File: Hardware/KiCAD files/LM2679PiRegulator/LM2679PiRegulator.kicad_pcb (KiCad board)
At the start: 2 copper layers, 48 x 48 mm, 14 parts, among them J2 Conn_01x03_Pin, U1 LM2679SX-5V

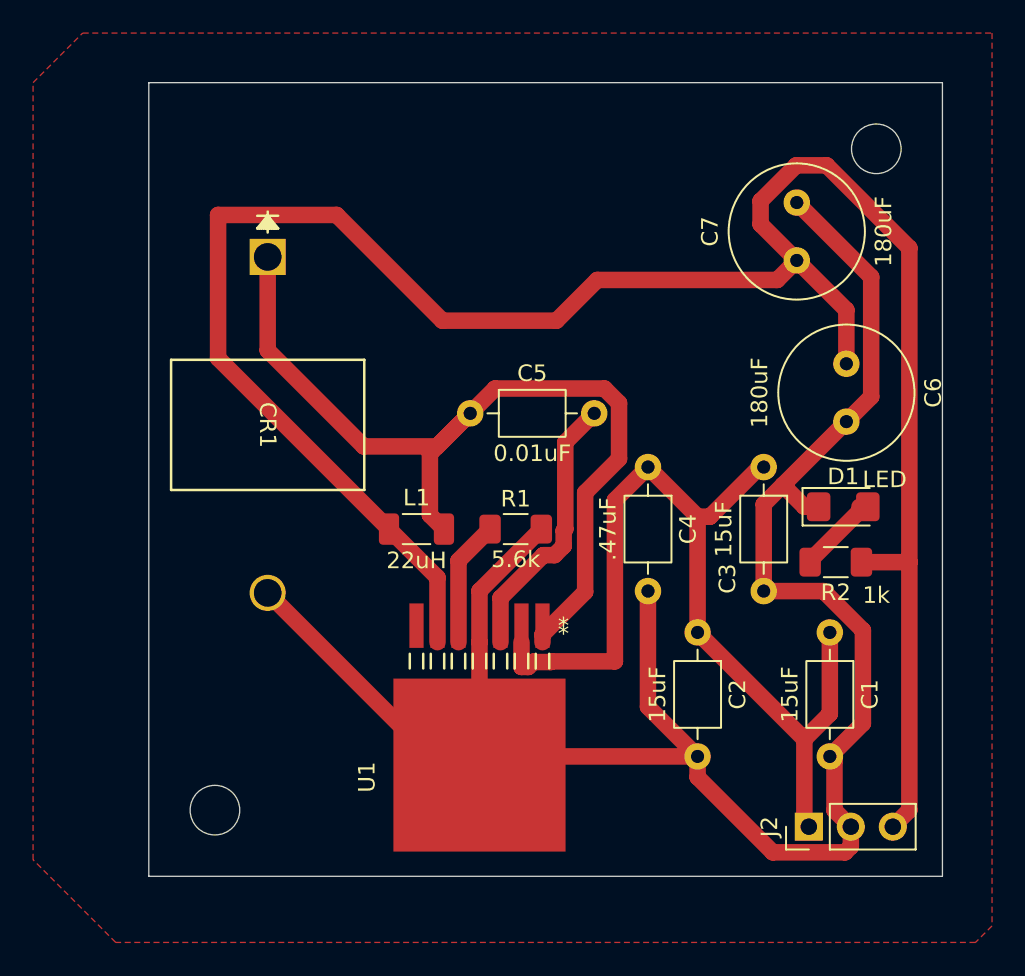
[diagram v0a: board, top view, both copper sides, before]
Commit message: 1st push of PCB's for printing
This is pre-peer review. This almost certainly has section that need adjustment. also realized I'm missing the USB-Uart bridge. first thing added in next version.
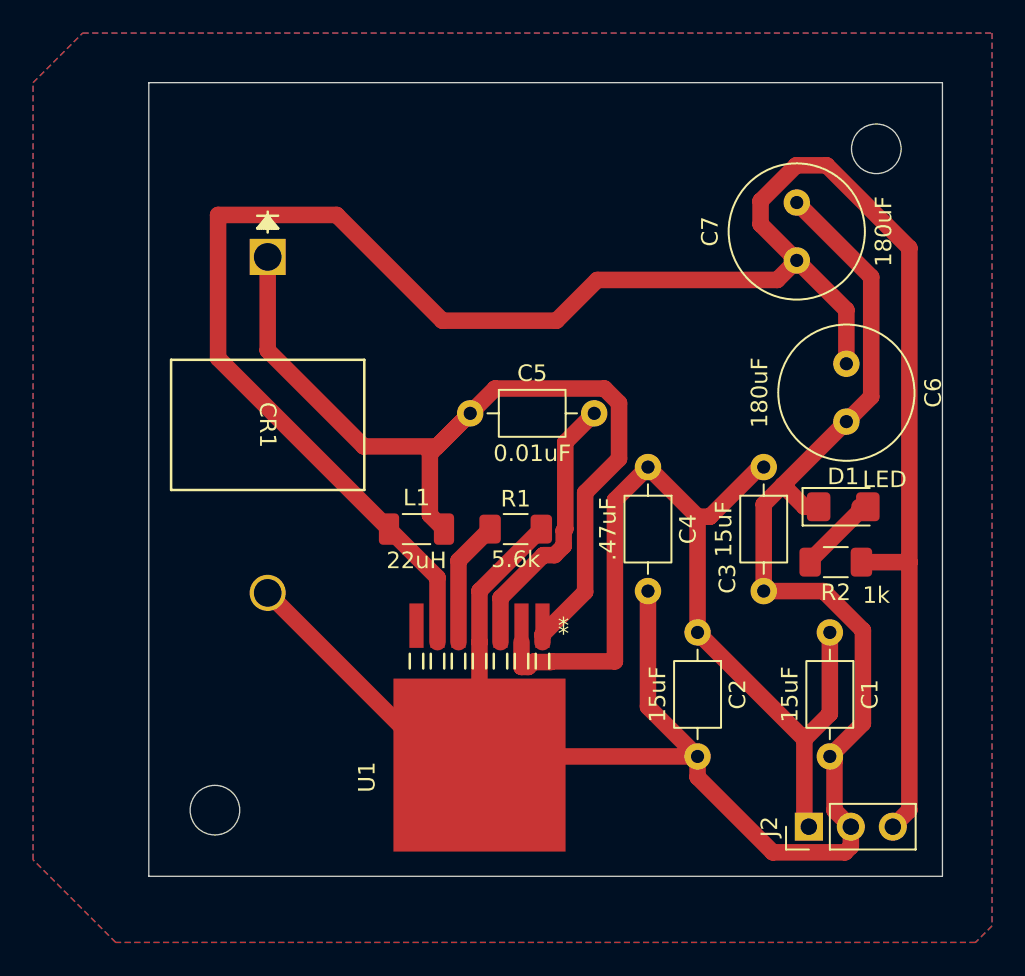
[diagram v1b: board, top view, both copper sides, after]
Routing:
- added copper zone on B.Cu, net GND

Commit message: general progress and adjustments
new footprint for pi reg inductor, var reg checked concurred with current part and value. re footprinted motor driver. started swapping head. adjusted some device footprints.
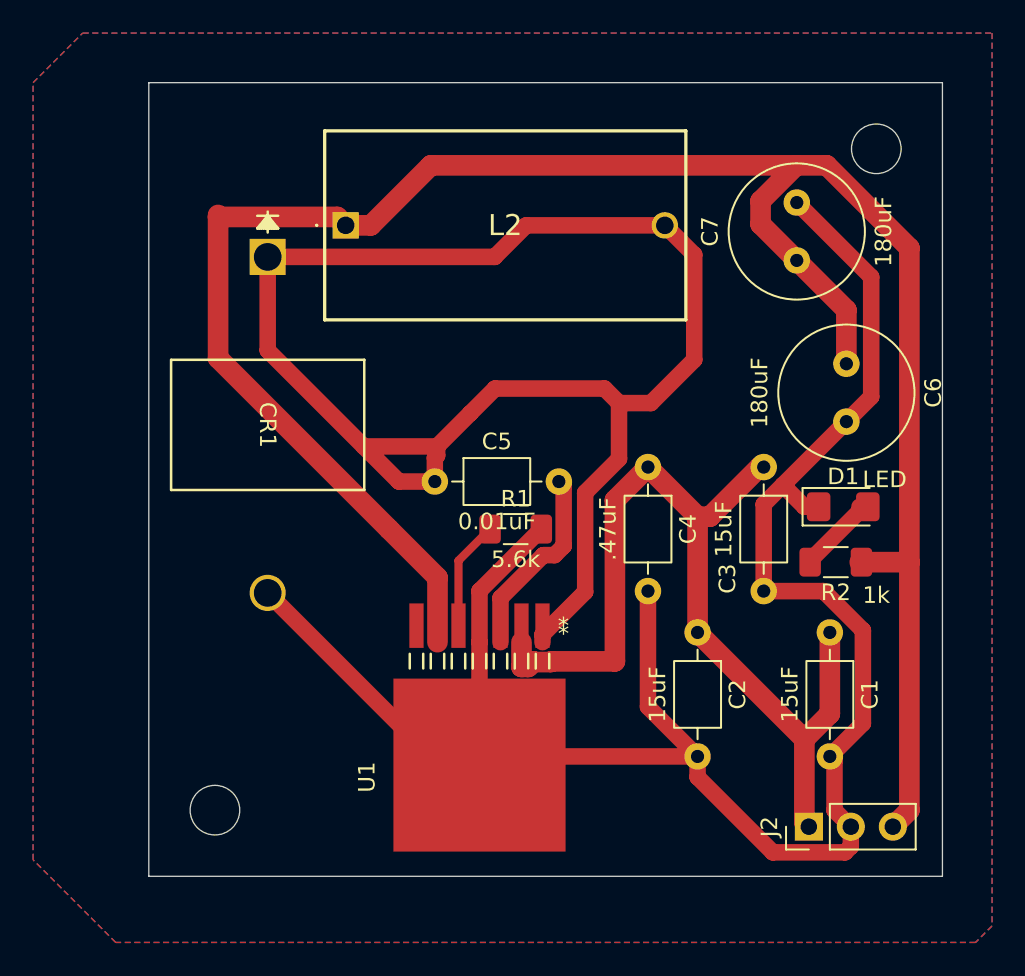
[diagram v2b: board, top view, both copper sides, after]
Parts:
- removed L1: 22uH, Inductor_SMD:L_1206_3216Metric_Pad1.22x1.90mm_HandSolder
- added L2: 2100LL-221H-RC, 2100LL-221H-RC:2100LL221HRC, F.Cu at (136.9, 87.6)
- moved C5 4.65 mm to (142.3, 103.1)
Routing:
- net /Switch: track 55.9 -> 94.2 mm
- net /Boost: track 16.6 -> 11.8 mm
- net /Vout: track 132.9 -> 130.4 mm

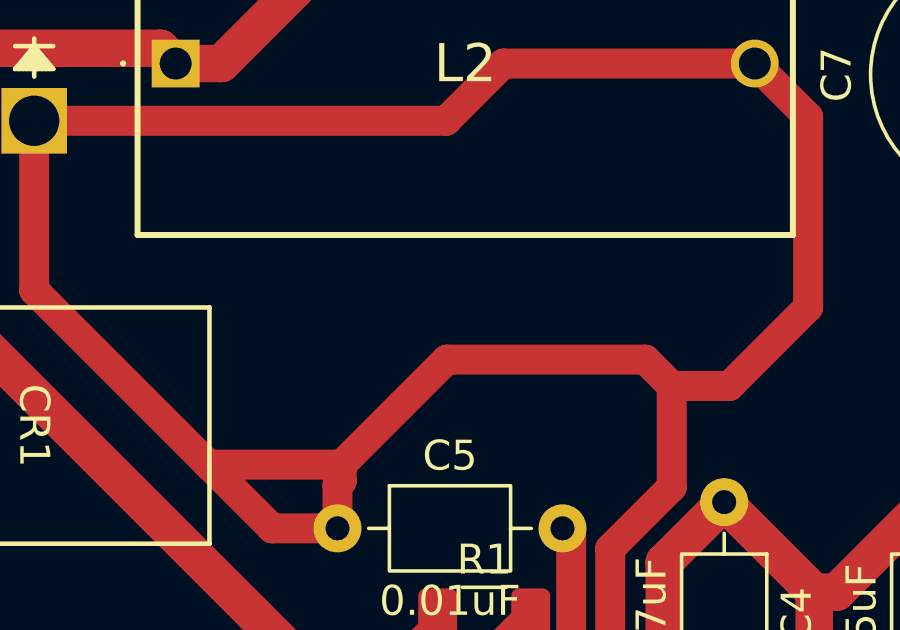
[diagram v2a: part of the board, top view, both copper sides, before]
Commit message: general updates to the schematics and layouts
includes some backchecks tot he master schematic to be accurate for the paper
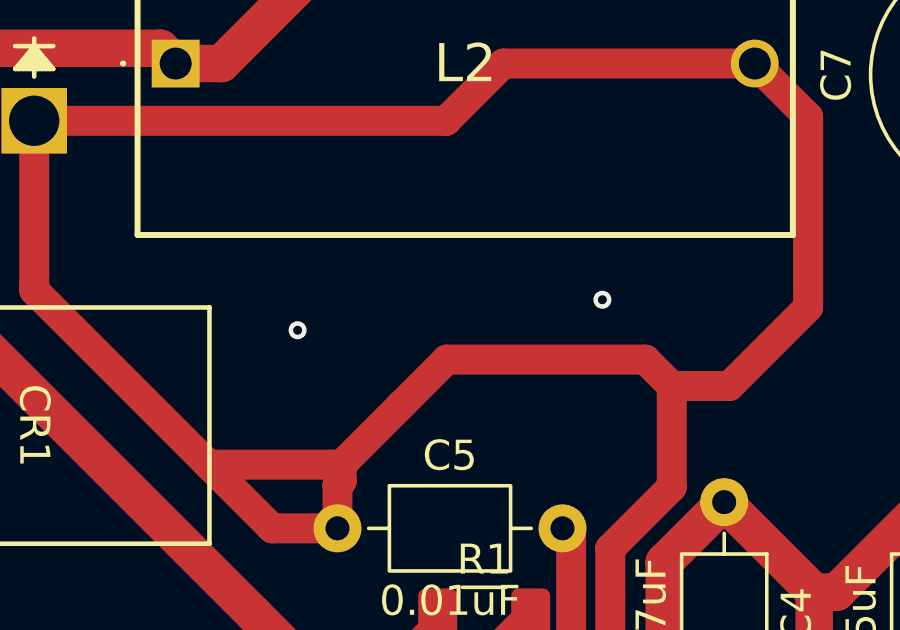
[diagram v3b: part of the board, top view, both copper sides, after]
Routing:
- net GND: vias 0 -> 2
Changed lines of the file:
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@@
+		(net "GND")
+	)
+	(via
+		(at 151.13 95.504)
+		(size 0.6)
+		(drill 0.3)
+		(layers "F.Cu" "B.Cu")
+		(free yes)
+		(net "GND")
+	)
+	(via
+		(at 140.97 96.52)
+		(size 0.6)
+		(drill 0.3)
+		(layers "F.Cu" "B.Cu")
+		(free yes)
 		(net "GND")
 	)

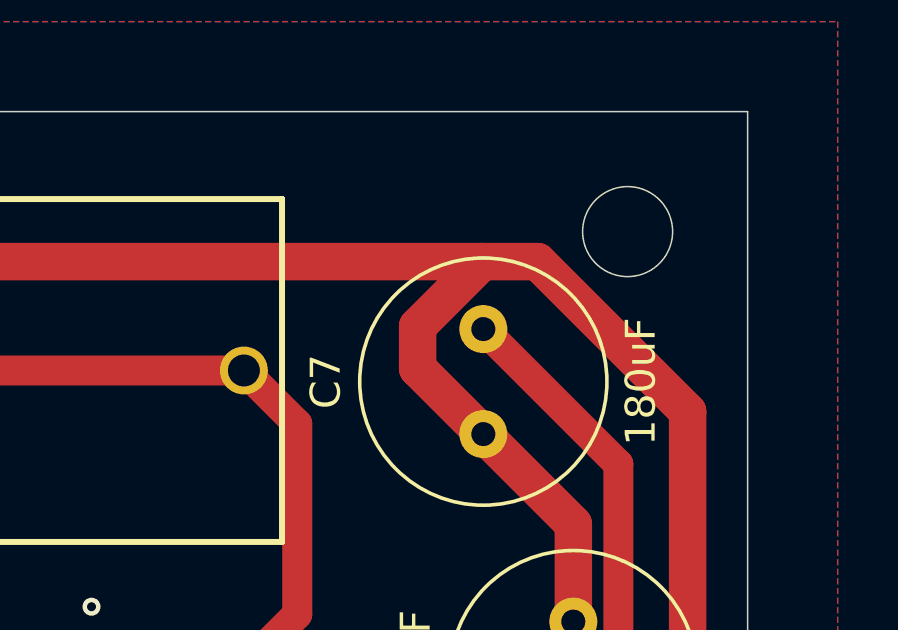
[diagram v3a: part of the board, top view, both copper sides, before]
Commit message: DRV 8825 and regulator purchased set
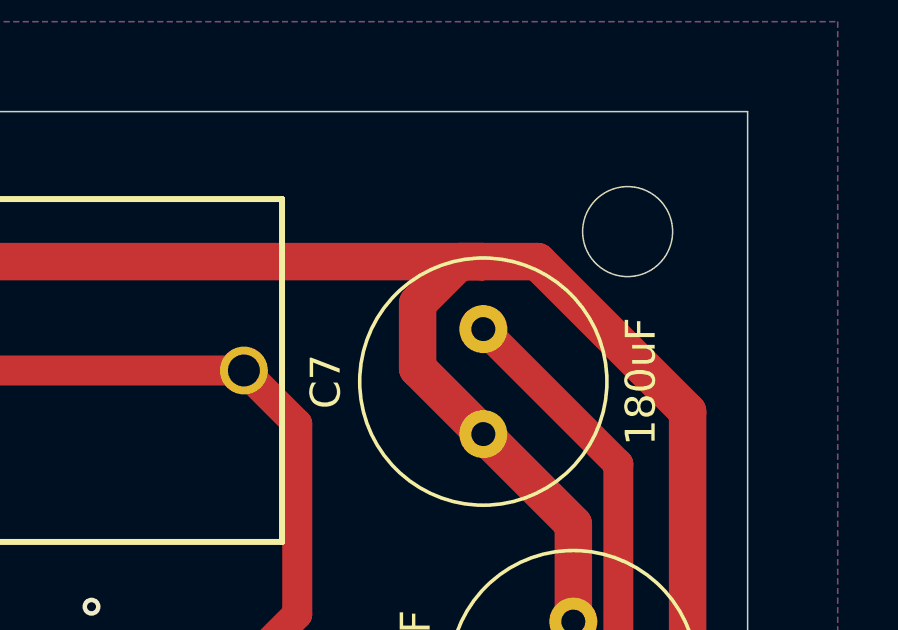
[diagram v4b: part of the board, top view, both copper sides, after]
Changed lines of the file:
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@@
 			(outputformat 1)
 			(mirror no)
-			(drillshape 1)
+			(drillshape 0)
 			(scaleselection 1)
-			(outputdirectory "")
+			(outputdirectory "../../manuracturing outputs/V1 boards/LM2679_Pi_Reg/")
 		)
 	)
@@
 	)
 	(segment
+		(start 163.396 84)
+		(end 162 85.396)
+		(width 1.25)
+		(layer "F.Cu")
+		(net "/Vout")
+	)
+	(segment
 		(start 136.906 87.63)
 		(end 138.43 87.63)
@@
 	)
 	(segment
-		(start 139.5275 106)
-		(end 129.19 95.6625)
+		(start 162 85.396)
+		(end 162 87.56)
 		(width 1.25)
 		(layer "F.Cu")
@@
 	)
 	(segment
-		(start 142.06 84)
-		(end 164.158633 84)
+		(start 162 87.56)
+		(end 164.19 89.75)
 		(width 1.25)
 		(layer "F.Cu")
@@
 	)
 	(segment
-		(start 171 108)
-		(end 171 89)
+		(start 139.5275 106)
+		(end 129.19 95.6625)
 		(width 1.25)
 		(layer "F.Cu")
@@
 	)
 	(segment
-		(start 164.158633 84)
-		(end 162 86.158633)
+		(start 142.06 84)
+		(end 164.158633 84)
 		(width 1.25)
 		(layer "F.Cu")
@@
 	)
 	(segment
-		(start 129.19 95.6625)
-		(end 129.19 87.122)
+		(start 171 108)
+		(end 171 89)
 		(width 1.25)
 		(layer "F.Cu")
@@
 	)
 	(segment
-		(start 162 86.158633)
-		(end 162 87.56)
+		(start 129.19 95.6625)
+		(end 129.19 87.122)
 		(width 1.25)
 		(layer "F.Cu")
@@
 	)
 	(segment
-		(start 162 87.56)
-		(end 164.19 89.75)
-		(width 1.25)
-		(layer "F.Cu")
-		(net "/Vout")
-	)
-	(segment
 		(start 168 108)
 		(end 171 108)
@@
 		(width 1.25)
 		(layer "F.Cu")
+		(net "/Vout")
+	)
+	(segment
+		(start 164.158633 84)
+		(end 163.396 84)
+		(width 1.25)
+		(layer "F.Cu")

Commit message: Most recent changes to final submission
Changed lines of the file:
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@@
-	)
-	(segment
-		(start 129.19 87.122)
-		(end 129.19 87)
-		(width 1.25)
-		(layer "F.Cu")
-		(net "/Vout")
 	)
 	(segment
